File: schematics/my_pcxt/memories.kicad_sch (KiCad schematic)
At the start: 13 parts, among them J2 Conn_02x40_Top_Bottom, U16 628128, U17 628128, U18 SST39SF040, U19 628128, U20 628128, U21 628128, U22 628128, U26 GAL16V8

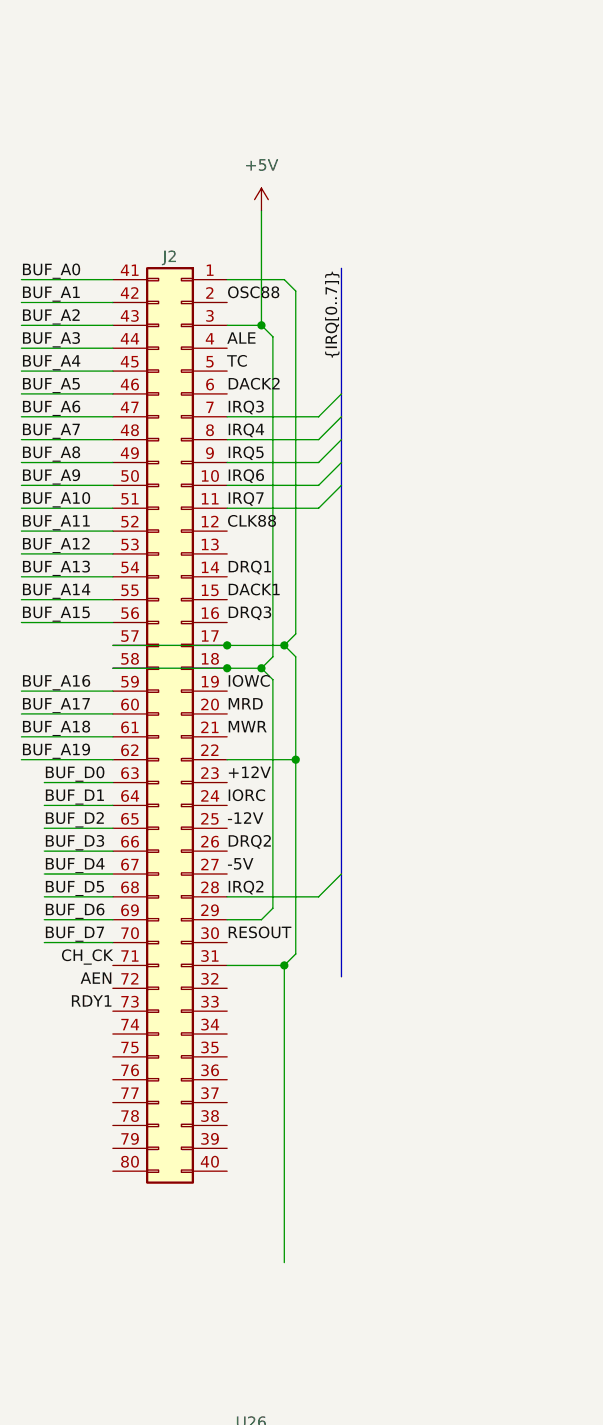
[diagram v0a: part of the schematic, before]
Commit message: Implemented 8259 e 8253
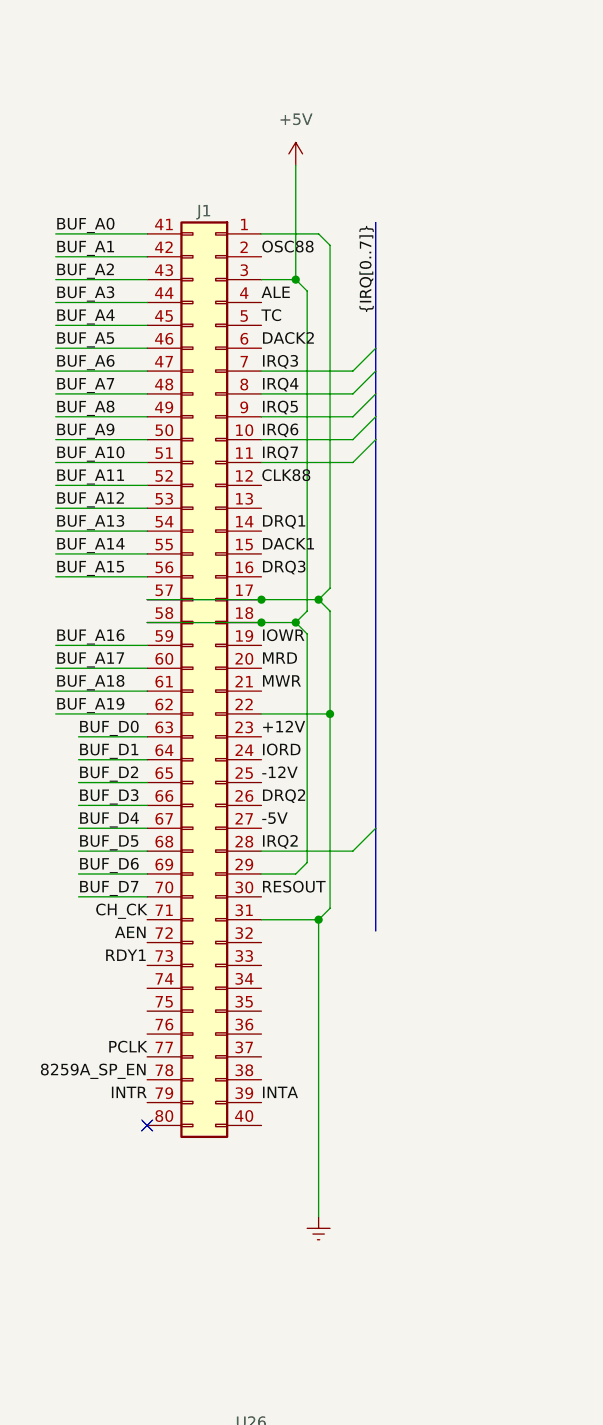
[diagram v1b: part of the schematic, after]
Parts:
- removed J2: Conn_02x40_Top_Bottom, symbol Connector_Generic:Conn_02x40_Top_Bottom
- added J1: Conn_02x40_Top_Bottom, symbol Connector_Generic:Conn_02x40_Top_Bottom
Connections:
- net +12V: now also J1.23 (Pin_23)
- net +5V: now also J1.18 (Pin_18), J1.29 (Pin_29), J1.3 (Pin_3), J1.58 (Pin_58)
- net -12V: now also J1.25 (Pin_25)
- net -5V: now also J1.27 (Pin_27)
- net AEN: now also J1.72 (Pin_72)
- net ALE: now also J1.4 (Pin_4)
- net BUF_A0: now also J1.41 (Pin_41)
- net BUF_A1: now also J1.42 (Pin_42)
- net BUF_A10: now also J1.51 (Pin_51)
- net BUF_A11: now also J1.52 (Pin_52)
- net BUF_A12: now also J1.53 (Pin_53)
- net BUF_A13: now also J1.54 (Pin_54)
- net BUF_A14: now also J1.55 (Pin_55)
- net BUF_A15: now also J1.56 (Pin_56)
- net BUF_A16: now also J1.59 (Pin_59)
- net BUF_A17: now also J1.60 (Pin_60)
- net BUF_A18: now also J1.61 (Pin_61)
- net BUF_A19: now also J1.62 (Pin_62)
- net BUF_A2: now also J1.43 (Pin_43)
- net BUF_A3: now also J1.44 (Pin_44)
- net BUF_A4: now also J1.45 (Pin_45)
- net BUF_A5: now also J1.46 (Pin_46)
- net BUF_A6: now also J1.47 (Pin_47)
- net BUF_A7: now also J1.48 (Pin_48)
- net BUF_A8: now also J1.49 (Pin_49)
- net BUF_A9: now also J1.50 (Pin_50)
- net BUF_D0: now also J1.63 (Pin_63)
- net BUF_D1: now also J1.64 (Pin_64)
- net BUF_D2: now also J1.65 (Pin_65)
- net BUF_D3: now also J1.66 (Pin_66)
- net BUF_D4: now also J1.67 (Pin_67)
- net BUF_D5: now also J1.68 (Pin_68)
- net BUF_D6: now also J1.69 (Pin_69)
- net BUF_D7: now also J1.70 (Pin_70)
- net CH_CK: now also J1.71 (Pin_71)
- net CLK88: now also J1.12 (Pin_12)
- net DACK1: now also J1.15 (Pin_15)
- net DACK2: now also J1.6 (Pin_6)
- net DRQ1: now also J1.14 (Pin_14)
- net DRQ2: now also J1.26 (Pin_26)
- net DRQ3: now also J1.16 (Pin_16)
- net IRQ2: now also J1.28 (Pin_28)
- net IRQ3: now also J1.7 (Pin_7)
- net IRQ4: now also J1.8 (Pin_8)
- net IRQ5: now also J1.9 (Pin_9)
- net IRQ6: now also J1.10 (Pin_10)
- net IRQ7: now also J1.11 (Pin_11)
- net MRD: now also J1.20 (Pin_20)
- net MWR: now also J1.21 (Pin_21)
- net OSC88: now also J1.2 (Pin_2)
- net RDY1: now also J1.73 (Pin_73)
- net RESOUT: now also J1.30 (Pin_30)
- net TC: now also J1.5 (Pin_5)
- new net 8259A_SP_EN: J1.78 (Pin_78)
- new net GNDREF: J1.1 (Pin_1), J1.17 (Pin_17), J1.22 (Pin_22), J1.31 (Pin_31), J1.57 (Pin_57)
- new net INTA: J1.39 (Pin_39)
- new net INTR: J1.79 (Pin_79)
- new net IORD: J1.24 (Pin_24)
- new net IOWR: J1.19 (Pin_19)
- new net PCLK: J1.77 (Pin_77)
- no-connect marks 1 -> 2

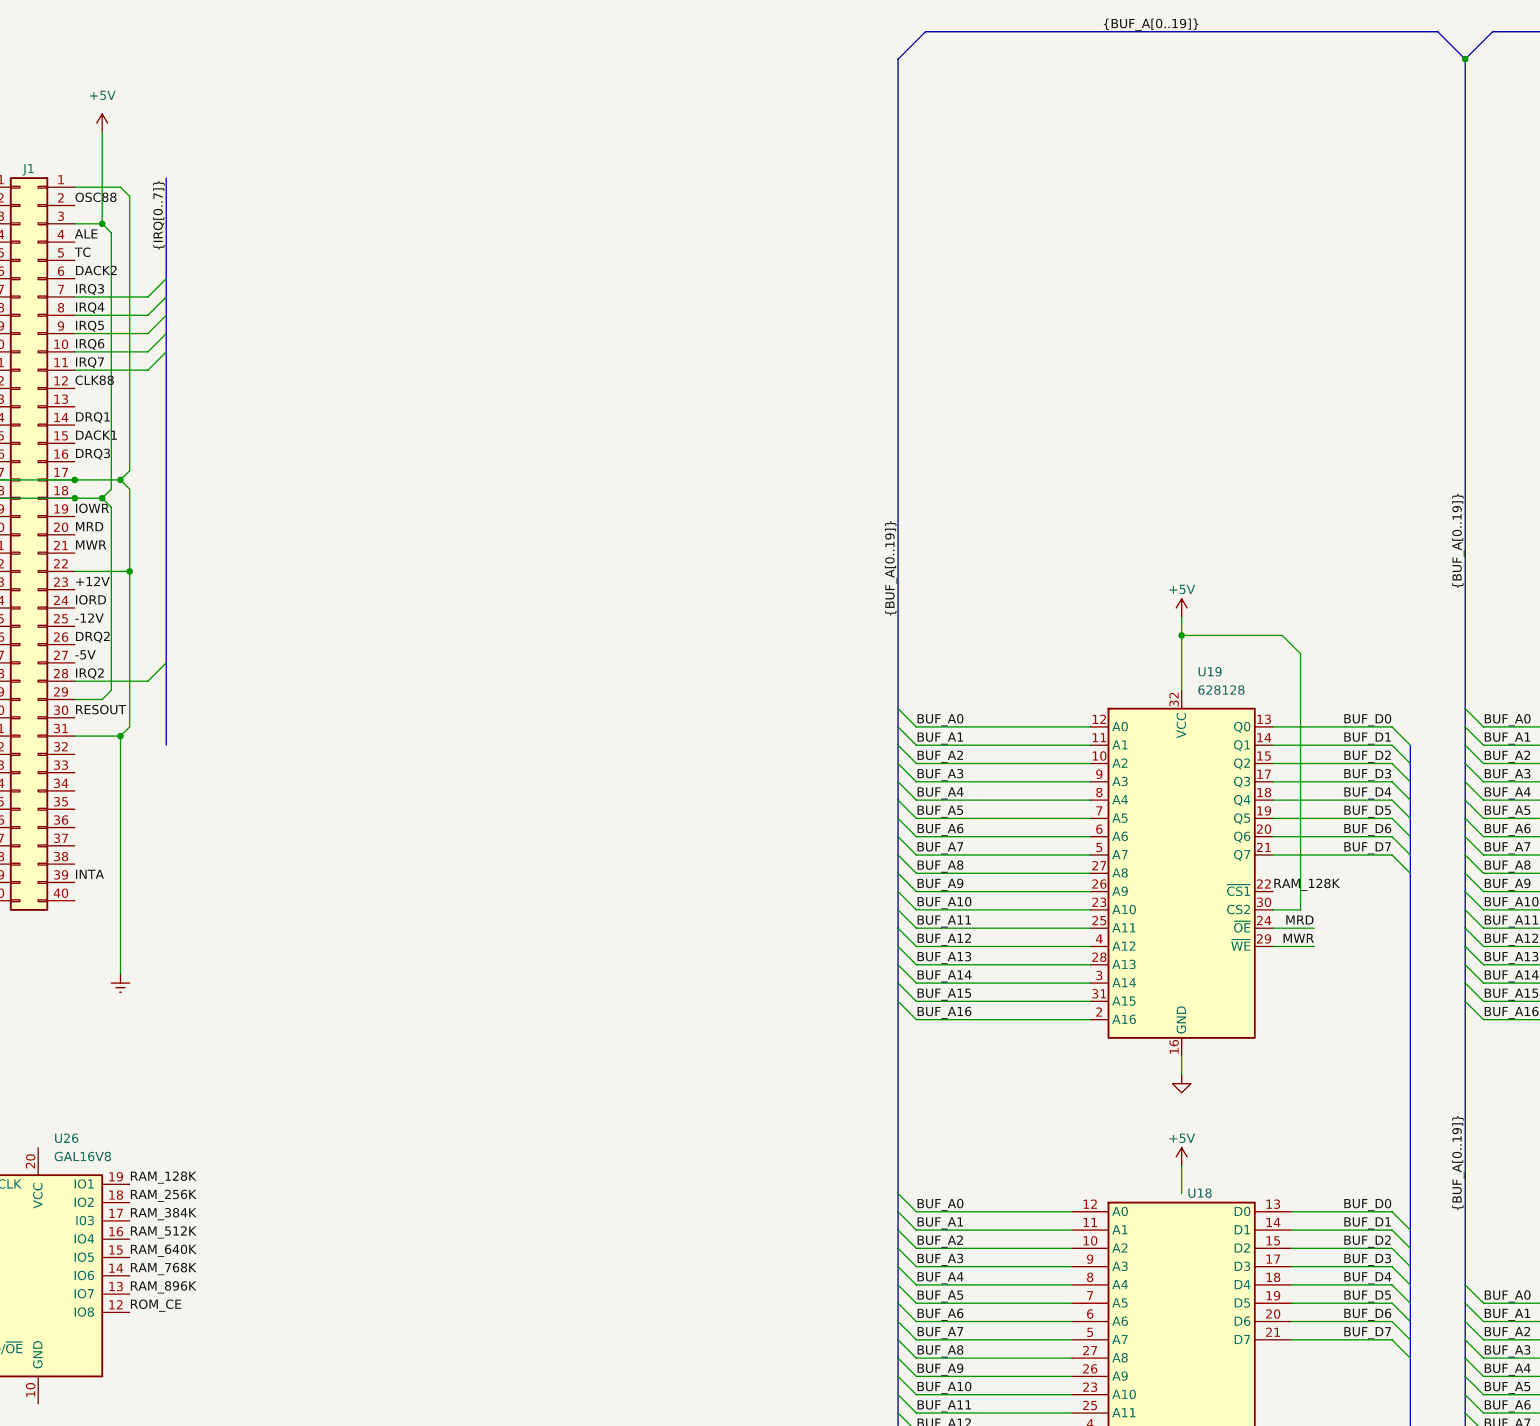
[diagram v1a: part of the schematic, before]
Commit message: Added IBM 5150 manual
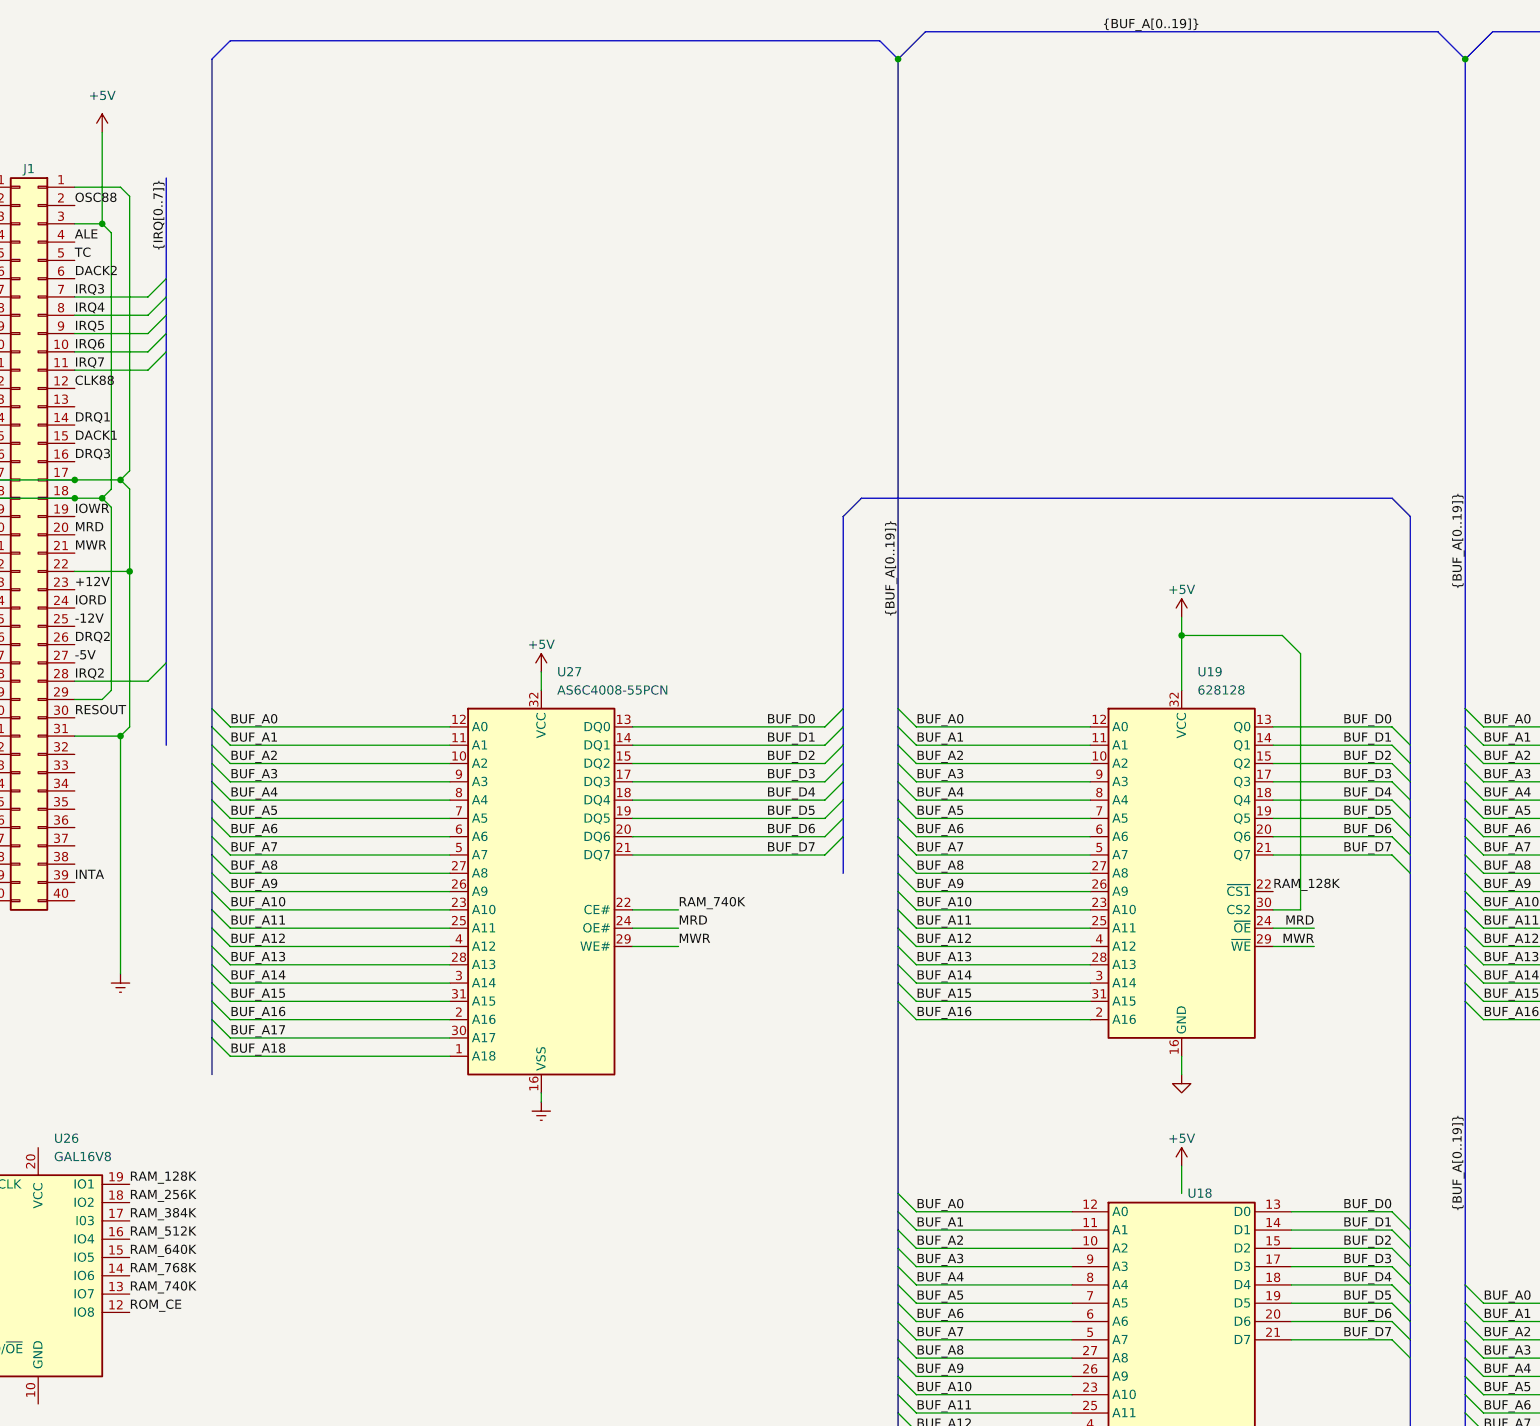
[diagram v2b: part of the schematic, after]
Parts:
- added U27: AS6C4008-55PCN, Package_DIP:DIP-32_W15.24mm, symbol Memory_RAM:AS6C4008-55PCN
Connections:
- net +5V: now also U27.32 (VCC)
- net BUF_A0: now also U27.12 (A0)
- net BUF_A1: now also U27.11 (A1)
- net BUF_A10: now also U27.23 (A10)
- net BUF_A11: now also U27.25 (A11)
- net BUF_A12: now also U27.4 (A12)
- net BUF_A13: now also U27.28 (A13)
- net BUF_A14: now also U27.3 (A14)
- net BUF_A15: now also U27.31 (A15)
- net BUF_A16: now also U27.2 (A16)
- net BUF_A17: now also U27.30 (A17)
- net BUF_A18: now also U27.1 (A18)
- net BUF_A2: now also U27.10 (A2)
- net BUF_A3: now also U27.9 (A3)
- net BUF_A4: now also U27.8 (A4)
- net BUF_A5: now also U27.7 (A5)
- net BUF_A6: now also U27.6 (A6)
- net BUF_A7: now also U27.5 (A7)
- net BUF_A8: now also U27.27 (A8)
- net BUF_A9: now also U27.26 (A9)
- net BUF_D0: now also U27.13 (DQ0)
- net BUF_D1: now also U27.14 (DQ1)
- net BUF_D2: now also U27.15 (DQ2)
- net BUF_D3: now also U27.17 (DQ3)
- net BUF_D4: now also U27.18 (DQ4)
- net BUF_D5: now also U27.19 (DQ5)
- net BUF_D6: now also U27.20 (DQ6)
- net BUF_D7: now also U27.21 (DQ7)
- net GNDREF: now also U27.16 (VSS)
- net MRD: now also U27.24 (OE#)
- net MWR: now also U27.29 (WE#)
- net RAM_896K renamed RAM_740K
- net RAM_740K: now also U27.22 (CE#)
